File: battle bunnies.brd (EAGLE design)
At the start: 151.7 x 94 mm, 59 parts, among them IC1 CP2104, Q1 mmbt2222, Q2 mmbt2222, SW2 KMR2, U1 PCA9685, U2 SPX3819, U3 MCP73831T-2ACI/OT, X2 ESP-12, X4 20329

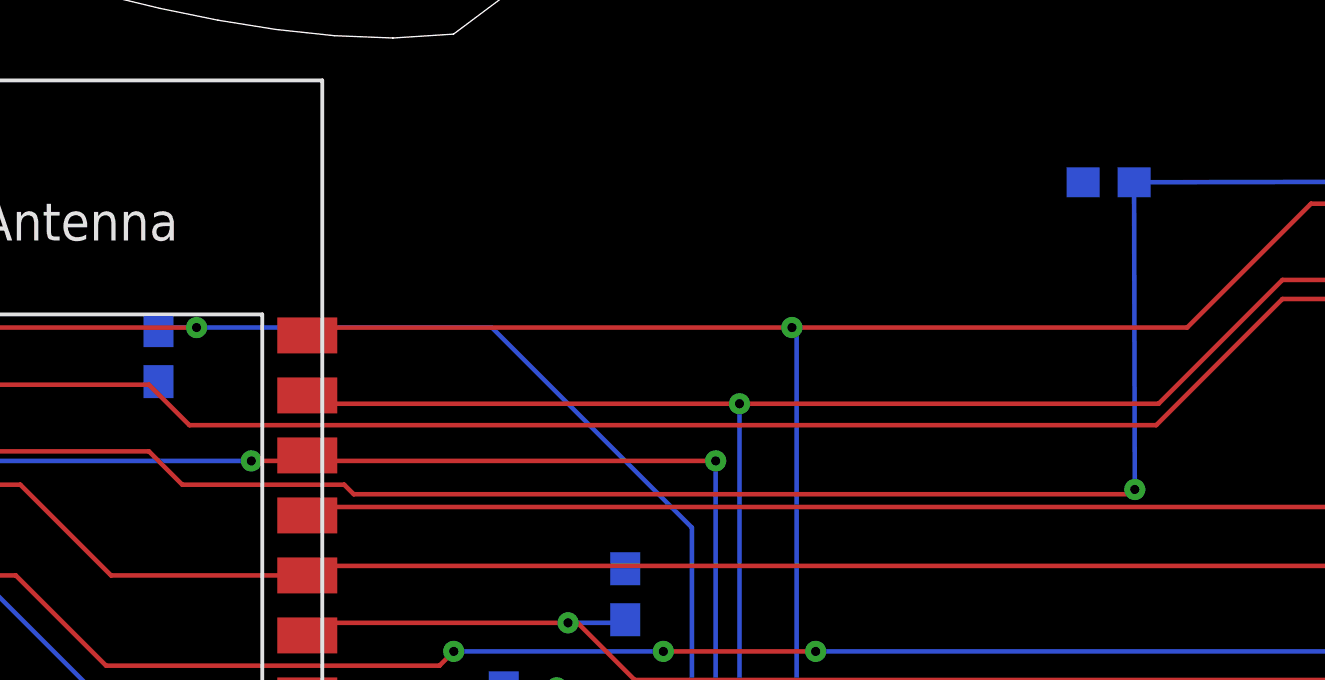
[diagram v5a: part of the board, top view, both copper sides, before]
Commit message: Adding values to the RNs that were missing
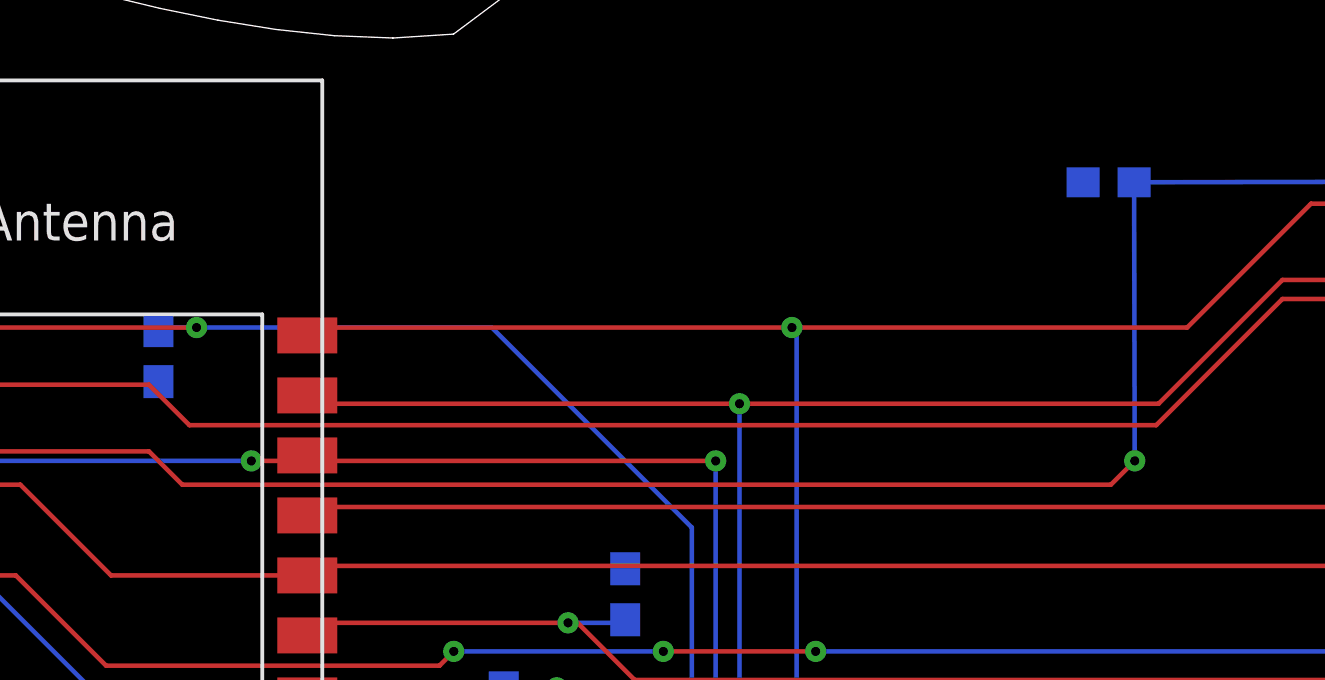
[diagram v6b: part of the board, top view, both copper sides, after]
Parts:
- RN3: value 10K -> 0
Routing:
- net CH_PD: track 109.0 -> 108.2 mm
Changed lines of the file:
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@@
 <attribute name="MF" value="" x="102.87" y="57.4675" size="0.17018125" layer="28" rot="MR90" display="off"/>
 </element>
-<element name="RN3" library="resistor-dil" package="EXB2HV" value="10K" x="89.8525" y="69.215" rot="MR0">
+<element name="RN3" library="resistor-dil" package="EXB2HV" value="0" x="89.8525" y="69.215" rot="MR0">
 <attribute name="OC_NEWARK" value="unknown" x="89.8525" y="69.215" size="0.17018125" layer="28" rot="MR0" display="off"/>
 <attribute name="MPN" value="" x="89.8525" y="69.215" size="0.17018125" layer="28" rot="MR0" display="off"/>
@@
 <wire x1="43.815" y1="65.0875" x2="34.2275" y2="65.0875" width="0.1524" layer="1"/>
 <wire x1="34.2275" y1="65.0875" x2="34.0925" y2="64.9525" width="0.1524" layer="1"/>
-<wire x1="50.64125" y1="63.65875" x2="76.5175" y2="63.65875" width="0.1524" layer="1"/>
-<via x="76.67625" y="63.8175" extent="1-16" drill="0.3048" diameter="0.3048"/>
-<wire x1="76.67625" y1="63.8175" x2="76.653125" y2="74.056875" width="0.1524" layer="16"/>
 <via x="88.5825" y="73.9775" extent="1-16" drill="0.3048" diameter="0.3048"/>
+<wire x1="76.674096875" y1="64.771071875" x2="76.653125" y2="74.056875" width="0.1524" layer="16"/>
 <wire x1="88.5825" y1="73.9775" x2="88.48" y2="74.08" width="0.1524" layer="16"/>
 <wire x1="88.48" y1="74.08" x2="76.653125" y2="74.056875" width="0.1524" layer="16"/>
@@
 <wire x1="122.8725" y1="81.28" x2="122.8725" y2="87.3125" width="0.1524" layer="16"/>
 <wire x1="43.815" y1="65.0875" x2="44.92625" y2="63.97625" width="0.1524" layer="1"/>
-<wire x1="44.92625" y1="63.97625" x2="50.32375" y2="63.97625" width="0.1524" layer="1"/>
-<wire x1="50.32375" y1="63.97625" x2="50.64125" y2="63.65875" width="0.1524" layer="1"/>
-<wire x1="76.67625" y1="63.8175" x2="76.5175" y2="63.65875" width="0.1524" layer="1"/>
+<wire x1="44.92625" y1="63.97625" x2="75.879275" y2="63.97625" width="0.1524" layer="1"/>
+<wire x1="75.879275" y1="63.97625" x2="76.674096875" y2="64.771071875" width="0.1524" layer="1"/>
+<via x="76.674096875" y="64.771071875" extent="1-16" drill="0.3048"/>
 </signal>
 <signal name="GPIO16">
